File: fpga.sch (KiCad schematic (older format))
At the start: 8 parts, among them U601 XC7A35T-FGG484, U602 S25FL127S

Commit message: specify FPGA speed grade
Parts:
- U601: value XC7A35T-FGG484 -> XC7A35T-2FGG484
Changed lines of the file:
@@
 P 19500 4600
 F 0 "U601" H 19500 1626 50  0000 C CNN
-F 1 "XC7A35T-FGG484" H 19500 1535 50  0000 C CNN
+F 1 "XC7A35T-2FGG484" H 19500 1535 50  0000 C CNN
 F 2 "Package_BGA:BGA-484_23.0x23.0mm_Layout22x22_P1.0mm" H 19500 4600 50  0001 C CNN
 F 3 "" H 19500 4600 50  0000 C CNN
@@
 P 8400 11100
 F 0 "U601" H 8350 9850 50  0000 L CNN
-F 1 "XC7A35T-FGG484" H 8100 9750 50  0000 L CNN
+F 1 "XC7A35T-2FGG484" H 8100 9750 50  0000 L CNN
 F 2 "Package_BGA:BGA-484_23.0x23.0mm_Layout22x22_P1.0mm" H 8400 11100 50  0001 C CNN
 F 3 "" H 8400 11100 50  0000 C CNN
@@
 P 8400 14600
 F 0 "U601" H 8400 15267 50  0000 C CNN
-F 1 "XC7A35T-FGG484" H 8400 15176 50  0000 C CNN
+F 1 "XC7A35T-2FGG484" H 8400 15176 50  0000 C CNN
 F 2 "Package_BGA:BGA-484_23.0x23.0mm_Layout22x22_P1.0mm" H 8400 14600 50  0001 C CNN
 F 3 "" H 8400 14600 50  0000 C CNN
@@
 P 13800 13600
 F 0 "U601" H 13850 11950 50  0000 R CNN
-F 1 "XC7A35T-FGG484" H 14100 11850 50  0000 R CNN
+F 1 "XC7A35T-2FGG484" H 14100 11850 50  0000 R CNN
 F 2 "Package_BGA:BGA-484_23.0x23.0mm_Layout22x22_P1.0mm" H 13800 13600 50  0001 C CNN
 F 3 "" H 13800 13600 50  0000 C CNN
@@
 P 2600 12500
 F 0 "U601" H 2600 15667 50  0000 C CNN
-F 1 "XC7A35T-FGG484" H 2600 15576 50  0000 C CNN
+F 1 "XC7A35T-2FGG484" H 2600 15576 50  0000 C CNN
 F 2 "Package_BGA:BGA-484_23.0x23.0mm_Layout22x22_P1.0mm" H 2600 12500 50  0001 C CNN
 F 3 "" H 2600 12500 50  0000 C CNN
@@
 P 5500 4600
 F 0 "U601" H 5550 1650 50  0000 R CNN
-F 1 "XC7A35T-FGG484" H 5800 1550 50  0000 R CNN
+F 1 "XC7A35T-2FGG484" H 5800 1550 50  0000 R CNN
 F 2 "Package_BGA:BGA-484_23.0x23.0mm_Layout22x22_P1.0mm" H 5500 4600 50  0001 C CNN
 F 3 "" H 5500 4600 50  0000 C CNN
@@
 P 12800 4600
 F 0 "U601" H 12800 1626 50  0000 C CNN
-F 1 "XC7A35T-FGG484" H 12800 1535 50  0000 C CNN
+F 1 "XC7A35T-2FGG484" H 12800 1535 50  0000 C CNN
 F 2 "Package_BGA:BGA-484_23.0x23.0mm_Layout22x22_P1.0mm" H 12800 4600 50  0001 C CNN
 F 3 "" H 12800 4600 50  0000 C CNN

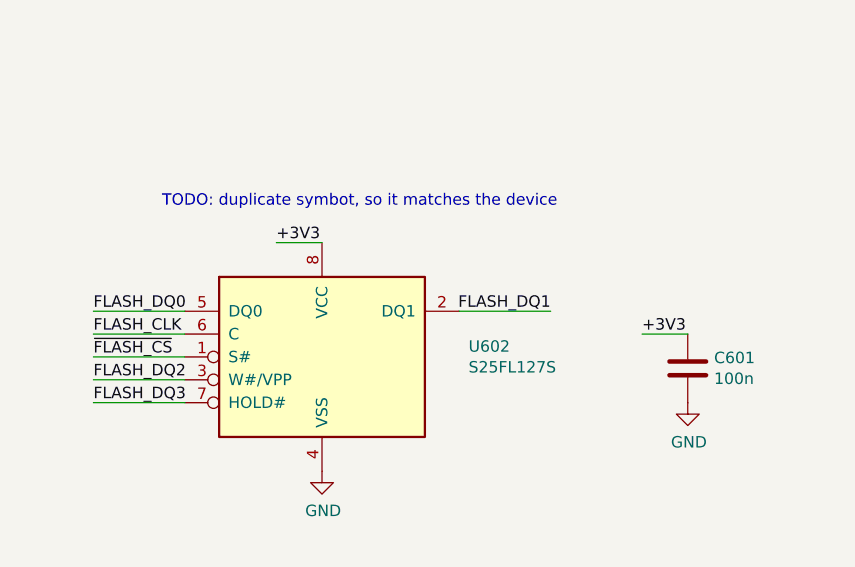
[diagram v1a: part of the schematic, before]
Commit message: specify exact part number of flash chip
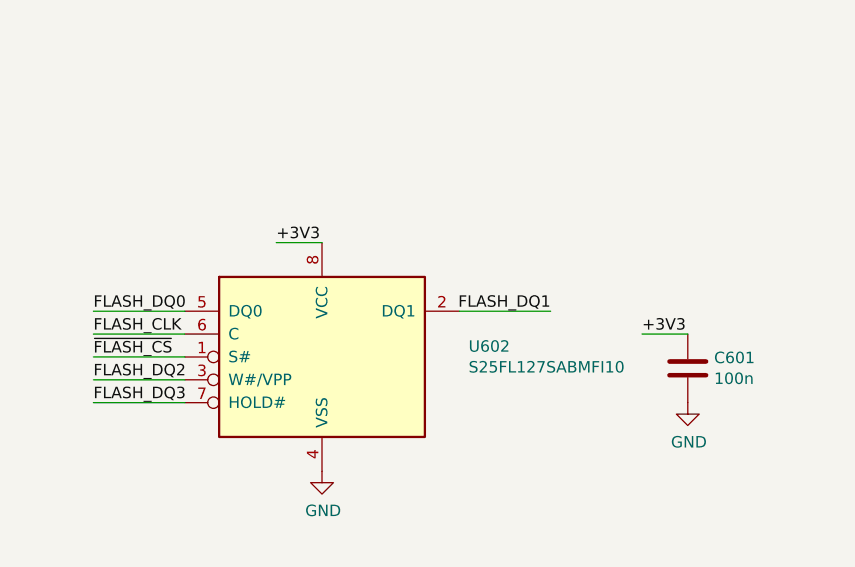
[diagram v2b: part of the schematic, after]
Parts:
- U602: value S25FL127S -> S25FL127SABMFI10
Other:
- note removed: "TODO: duplicate symbot, so it matches the device"
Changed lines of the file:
@@
 P 19500 12300
 F 0 "U602" H 20141 12346 50  0000 L CNN
-F 1 "S25FL127S" H 20141 12255 50  0000 L CNN
+F 1 "S25FL127SABMFI10" H 20141 12255 50  0000 L CNN
 F 2 "Package_SO:SOIJ-8_5.3x5.3mm_P1.27mm" H 20150 12350 50  0001 C CNN
-F 3 "https://www.micron.com/~/media/documents/products/data-sheet/nor-flash/serial-nor/m25px/m25px32.pdf" H 19650 12200 50  0001 C CNN
+F 3 "" H 19650 12200 50  0001 C CNN
 	1    19500 12300
 	1    0    0    -1
@@
 Wire Wire Line
 	21500 5200 21600 5200
-Text Notes 18800 11650 0    50   ~ 0
-TODO: duplicate symbot, so it matches the device
 NoConn ~ 21500 3300
 NoConn ~ 21500 3700

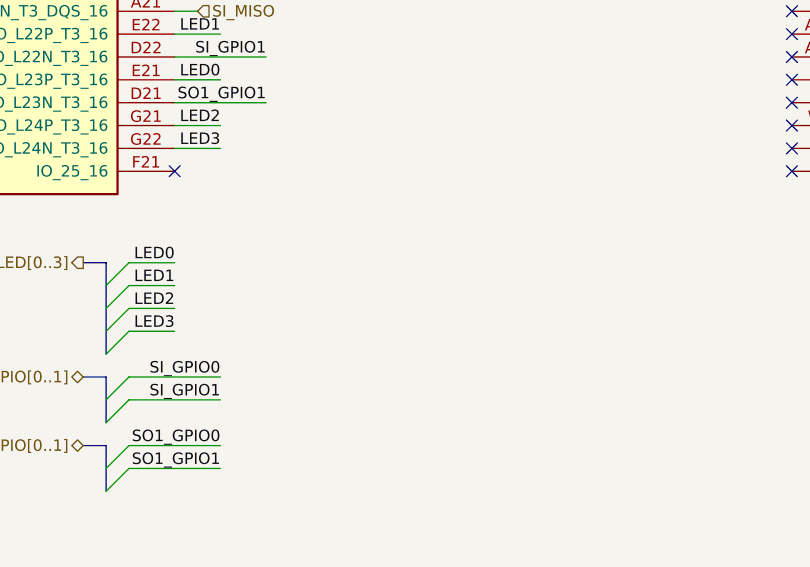
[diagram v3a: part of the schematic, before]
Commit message: connect leds to 3v3 power supply rail
the led is still connected to a 1v8 fpga io bank though
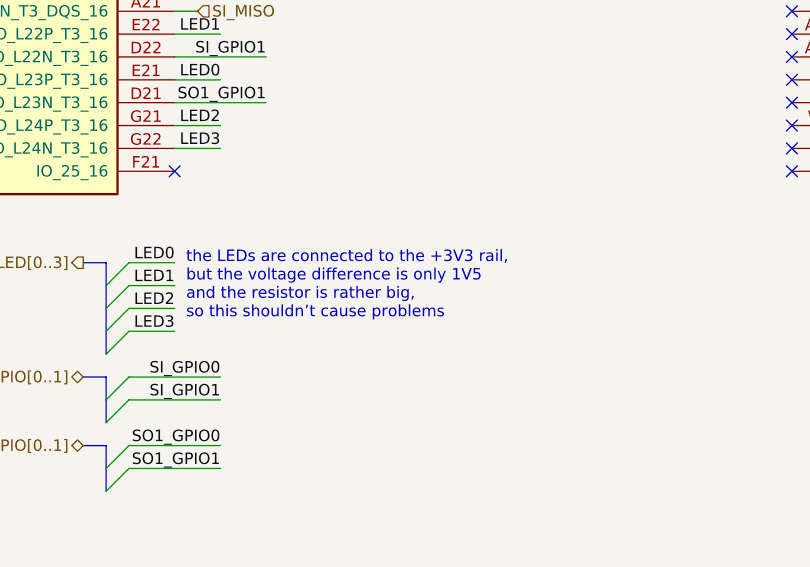
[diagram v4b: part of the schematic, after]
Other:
- note added: "the LEDs are connected to the +3V3 rail,\nbut the voltage difference is only 1V5\nand the resistor is rather big,\nso this shouldn’t cause problems"
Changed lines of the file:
@@
 Wire Bus Line
 	14500 7800 14500 8200
+Text Notes 14850 8050 0    50   ~ 0
+the LEDs are connected to the +3V3 rail,\nbut the voltage difference is only 1V5\nand the resistor is rather big,\nso this shouldn’t cause problems
 $EndSCHEMATC

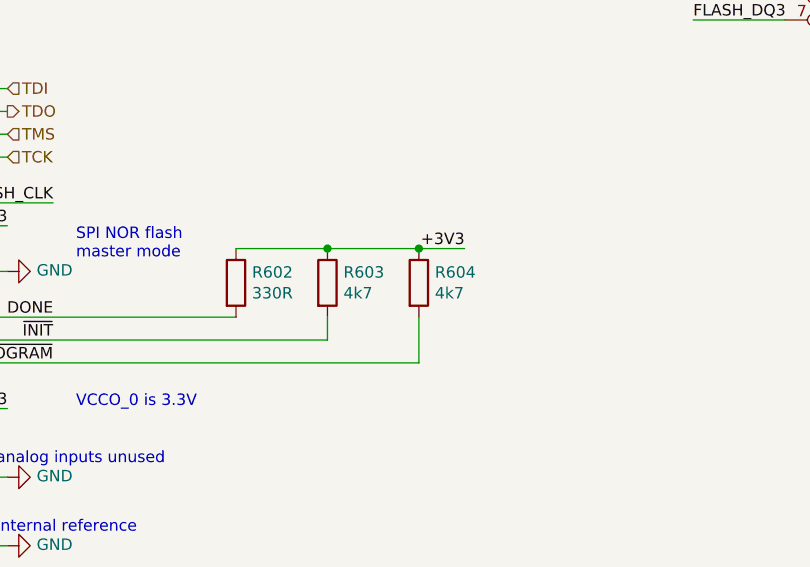
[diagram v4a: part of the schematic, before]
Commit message: fix moved plane bug, add init, done and power enable signals and optimize design
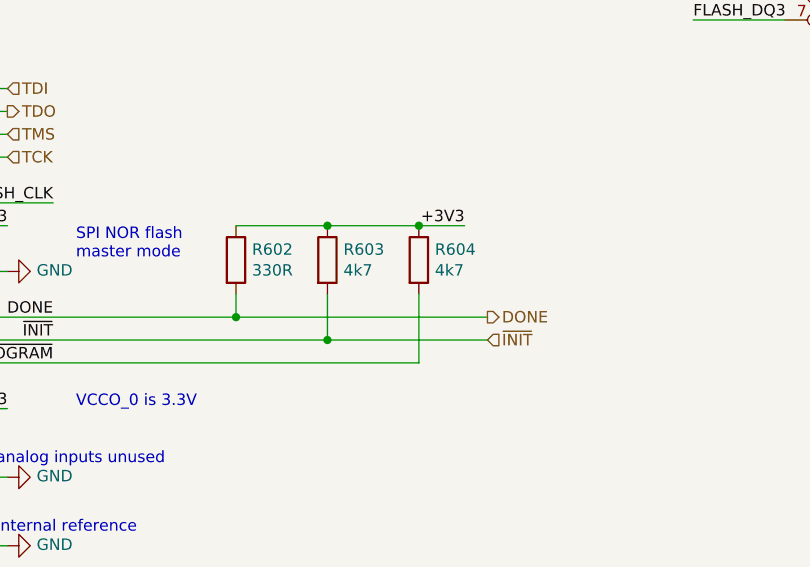
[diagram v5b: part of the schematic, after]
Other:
- moved on the sheet: R602, R603, R604
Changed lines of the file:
@@
 L Device:R R602
 U 1 1 5B3AC428
-P 16500 13650
-F 0 "R602" H 16570 13696 50  0000 L CNN
-F 1 "330R" H 16570 13605 50  0000 L CNN
-F 2 "Resistor_SMD:R_0402_1005Metric" V 16430 13650 50  0001 C CNN
-F 3 "~" H 16500 13650 50  0001 C CNN
-	1    16500 13650
+P 16500 13550
+F 0 "R602" H 16570 13596 50  0000 L CNN
+F 1 "330R" H 16570 13505 50  0000 L CNN
+F 2 "Resistor_SMD:R_0402_1005Metric" V 16430 13550 50  0001 C CNN
+F 3 "~" H 16500 13550 50  0001 C CNN
+	1    16500 13550
 	1    0    0    -1
 $EndComp
-Wire Wire Line
-	15300 13800 16500 13800
 $Comp
 L Device:R R603
 U 1 1 5B3F3344
-P 16900 13650
-F 0 "R603" H 16970 13696 50  0000 L CNN
-F 1 "4k7" H 16970 13605 50  0000 L CNN
-F 2 "Resistor_SMD:R_0402_1005Metric" V 16830 13650 50  0001 C CNN
-F 3 "~" H 16900 13650 50  0001 C CNN
-	1    16900 13650
+P 16900 13550
+F 0 "R603" H 16970 13596 50  0000 L CNN
+F 1 "4k7" H 16970 13505 50  0000 L CNN
+F 2 "Resistor_SMD:R_0402_1005Metric" V 16830 13550 50  0001 C CNN
+F 3 "~" H 16900 13550 50  0001 C CNN
+	1    16900 13550
 	1    0    0    -1
 $EndComp
@@
 L Device:R R604
 U 1 1 5B416F10
-P 17300 13650
-F 0 "R604" H 17370 13696 50  0000 L CNN
-F 1 "4k7" H 17370 13605 50  0000 L CNN
-F 2 "Resistor_SMD:R_0402_1005Metric" V 17230 13650 50  0001 C CNN
-F 3 "~" H 17300 13650 50  0001 C CNN
-	1    17300 13650
+P 17300 13550
+F 0 "R604" H 17370 13596 50  0000 L CNN
+F 1 "4k7" H 17370 13505 50  0000 L CNN
+F 2 "Resistor_SMD:R_0402_1005Metric" V 17230 13550 50  0001 C CNN
+F 3 "~" H 17300 13550 50  0001 C CNN
+	1    17300 13550
 	1    0    0    -1
 $EndComp
@@
 +1V0
 Wire Wire Line
-	16500 13500 16900 13500
-Wire Wire Line
-	16900 13500 17300 13500
-Connection ~ 16900 13500
-Wire Wire Line
-	17300 13500 17500 13500
-Connection ~ 17300 13500
-Text Label 17500 13500 2    50   ~ 0
-+3V3
-Wire Wire Line
-	16900 13900 16900 13800
-Wire Wire Line
-	17300 14000 17300 13800
+	16500 13400 16900 13400
+Wire Wire Line
+	16900 13400 17300 13400
+Connection ~ 16900 13400
+Wire Wire Line
+	17300 13400 17500 13400
+Connection ~ 17300 13400
+Text Label 17500 13400 2    50   ~ 0
++3V3
+Wire Wire Line
+	16900 13900 16900 13700
+Wire Wire Line
+	17300 14000 17300 13700
 Text Label 14600 11900 0    50   ~ 0
 +3V3
@@
 Wire Wire Line
 	21500 6700 21600 6700
-Wire Bus Line
-	14500 8600 14500 8800
-Wire Bus Line
-	21000 7800 21000 8000
-Wire Bus Line
-	14500 8300 14500 8500
-Wire Bus Line
-	14500 7800 14500 8200
 Text Notes 14850 8050 0    50   ~ 0
 the LEDs are connected to the +3V3 rail,\nbut the voltage difference is only 1V5\nand the resistor is rather big,\nso this shouldn’t cause problems
+Text HLabel 17600 13900 2    50   Input ~ 0
+~INIT
+Wire Wire Line
+	16900 13900 17600 13900
+Connection ~ 16900 13900
+Text HLabel 17600 13800 2    50   Output ~ 0
+DONE
+Wire Wire Line
+	15300 13800 16500 13800
+Wire Wire Line
+	16500 13700 16500 13800
+Connection ~ 16500 13800
+Wire Wire Line
+	16500 13800 17600 13800
+Wire Bus Line
+	14500 8600 14500 8800
+Wire Bus Line
+	21000 7800 21000 8000
+Wire Bus Line
+	14500 8300 14500 8500
+Wire Bus Line
+	14500 7800 14500 8200
 $EndSCHEMATC

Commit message: add 3 resistor footprints to configure a board ID to be able to detect revision and features present
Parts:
- added R602, R603, R604: 100R, Resistor_SMD:R_0402_1005Metric, symbol Device:R
- renumbered R602 to R605, R603 to R606, R604 to R607, R605 to R608
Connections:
- net GND: now also R602.1, R603.1, R604.1
- net BOARD_ID_2: now reaches U601.V18 (IO_L14P_T2_SRCC_14)
- net BOARD_ID_2: now also R604.2
- net BOARD_ID_1: now reaches U601.Y18 (IO_L13P_T2_MRCC_14)
- net BOARD_ID_1: now also R602.2
- net BOARD_ID_0: now reaches U601.Y19 (IO_L13N_T2_MRCC_14)
- net BOARD_ID_0: now also R603.2
- no-connect marks 190 -> 187
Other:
- note added: "populate these depending on the board ID"
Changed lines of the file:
@@
 $EndComp
 $Comp
-L power:GND #PWR0613
+L power:GND #PWR0616
 U 1 1 5AEC478C
 P 1500 15500
-F 0 "#PWR0613" H 1500 15250 50  0001 C CNN
+F 0 "#PWR0616" H 1500 15250 50  0001 C CNN
 F 1 "GND" H 1505 15327 50  0000 C CNN
 F 2 "" H 1500 15500 50  0001 C CNN
@@
 	1500 15400 1500 15500
 $Comp
-L power:GND #PWR0614
+L power:GND #PWR0617
 U 1 1 5AED823A
 P 3700 15500
-F 0 "#PWR0614" H 3700 15250 50  0001 C CNN
+F 0 "#PWR0617" H 3700 15250 50  0001 C CNN
 F 1 "GND" H 3705 15327 50  0000 C CNN
 F 2 "" H 3700 15500 50  0001 C CNN
@@
 	3700 15400 3700 15500
 $Comp
-L Device:R R605
+L Device:R R608
 U 1 1 5AF685FD
 P 10650 14900
-F 0 "R605" V 10443 14900 50  0000 C CNN
+F 0 "R608" V 10443 14900 50  0000 C CNN
 F 1 "100R" V 10534 14900 50  0000 C CNN
 F 2 "Resistor_SMD:R_0201_0603Metric" V 10580 14900 50  0001 C CNN
@@
 	15300 13400 15500 13400
 $Comp
-L power:GND #PWR0610
+L power:GND #PWR0613
 U 1 1 5B037925
 P 15500 13600
-F 0 "#PWR0610" H 15500 13350 50  0001 C CNN
+F 0 "#PWR0613" H 15500 13350 50  0001 C CNN
 F 1 "GND" V 15505 13472 50  0000 R CNN
 F 2 "" H 15500 13600 50  0001 C CNN
@@
 NoConn ~ 14800 3300
 $Comp
-L power:GND #PWR0606
+L power:GND #PWR0609
 U 1 1 5B5B64DE
 P 6800 11500
-F 0 "#PWR0606" H 6800 11250 50  0001 C CNN
+F 0 "#PWR0609" H 6800 11250 50  0001 C CNN
 F 1 "GND" V 6805 11372 50  0000 R CNN
 F 2 "" H 6800 11500 50  0001 C CNN
@@
 $EndComp
 $Comp
-L power:GND #PWR0607
+L power:GND #PWR0610
 U 1 1 5B5B6565
 P 6800 11600
-F 0 "#PWR0607" H 6800 11350 50  0001 C CNN
+F 0 "#PWR0610" H 6800 11350 50  0001 C CNN
 F 1 "GND" V 6805 11472 50  0000 R CNN
 F 2 "" H 6800 11600 50  0001 C CNN
@@
 $EndComp
 $Comp
-L power:GND #PWR0604
+L power:GND #PWR0607
 U 1 1 5B5B6582
 P 6800 11100
-F 0 "#PWR0604" H 6800 10850 50  0001 C CNN
+F 0 "#PWR0607" H 6800 10850 50  0001 C CNN
 F 1 "GND" V 6805 10972 50  0000 R CNN
 F 2 "" H 6800 11100 50  0001 C CNN
@@
 $EndComp
 $Comp
-L power:GND #PWR0605
+L power:GND #PWR0608
 U 1 1 5B5B659F
 P 6800 11200
-F 0 "#PWR0605" H 6800 10950 50  0001 C CNN
+F 0 "#PWR0608" H 6800 10950 50  0001 C CNN
 F 1 "GND" V 6805 11072 50  0000 R CNN
 F 2 "" H 6800 11200 50  0001 C CNN
@@
 $EndComp
 $Comp
-L power:GND #PWR0609
+L power:GND #PWR0612
 U 1 1 5AFE504F
 P 19500 12800
-F 0 "#PWR0609" H 19500 12550 50  0001 C CNN
+F 0 "#PWR0612" H 19500 12550 50  0001 C CNN
 F 1 "GND" H 19505 12627 50  0000 C CNN
 F 2 "" H 19500 12800 50  0001 C CNN
@@
 $EndComp
 $Comp
-L power:GND #PWR0608
+L power:GND #PWR0611
 U 1 1 5AFE56CA
 P 21100 12500
-F 0 "#PWR0608" H 21100 12250 50  0001 C CNN
+F 0 "#PWR0611" H 21100 12250 50  0001 C CNN
 F 1 "GND" H 21105 12327 50  0000 C CNN
 F 2 "" H 21100 12500 50  0001 C CNN
@@
 ~FLASH_CS
 $Comp
-L power:GND #PWR0612
+L power:GND #PWR0615
 U 1 1 5B0155B6
 P 15500 14800
-F 0 "#PWR0612" H 15500 14550 50  0001 C CNN
+F 0 "#PWR0615" H 15500 14550 50  0001 C CNN
 F 1 "GND" V 15505 14672 50  0000 R CNN
 F 2 "" H 15500 14800 50  0001 C CNN
@@
 internal reference
 $Comp
-L power:GND #PWR0602
+L power:GND #PWR0605
 U 1 1 5B074A2B
 P 1400 10200
-F 0 "#PWR0602" H 1400 9950 50  0001 C CNN
+F 0 "#PWR0605" H 1400 9950 50  0001 C CNN
 F 1 "GND" V 1405 10072 50  0000 R CNN
 F 2 "" H 1400 10200 50  0001 C CNN
@@
 	1600 10200 1400 10200
 $Comp
-L power:GND #PWR0611
+L power:GND #PWR0614
 U 1 1 5B0BD6A0
 P 15500 14500
-F 0 "#PWR0611" H 15500 14250 50  0001 C CNN
+F 0 "#PWR0614" H 15500 14250 50  0001 C CNN
 F 1 "GND" V 15505 14372 50  0000 R CNN
 F 2 "" H 15500 14500 50  0001 C CNN
@@
 NoConn ~ 7500 5700
 $Comp
-L power:GND #PWR0603
+L power:GND #PWR0606
 U 1 1 5B267380
 P 1400 10400
-F 0 "#PWR0603" H 1400 10150 50  0001 C CNN
+F 0 "#PWR0606" H 1400 10150 50  0001 C CNN
 F 1 "GND" V 1405 10272 50  0000 R CNN
 F 2 "" H 1400 10400 50  0001 C CNN
@@
 ~PROGRAM
 $Comp
-L Device:R R602
+L Device:R R605
 U 1 1 5B3AC428
 P 16500 13550
-F 0 "R602" H 16570 13596 50  0000 L CNN
+F 0 "R605" H 16570 13596 50  0000 L CNN
 F 1 "330R" H 16570 13505 50  0000 L CNN
 F 2 "Resistor_SMD:R_0402_1005Metric" V 16430 13550 50  0001 C CNN
@@
 $EndComp
 $Comp
-L Device:R R603
+L Device:R R606
 U 1 1 5B3F3344
 P 16900 13550
-F 0 "R603" H 16970 13596 50  0000 L CNN
+F 0 "R606" H 16970 13596 50  0000 L CNN
 F 1 "4k7" H 16970 13505 50  0000 L CNN
 F 2 "Resistor_SMD:R_0402_1005Metric" V 16830 13550 50  0001 C CNN
@@
 	15300 13900 16900 13900
 $Comp
-L Device:R R604
+L Device:R R607
 U 1 1 5B416F10
 P 17300 13550
-F 0 "R604" H 17370 13596 50  0000 L CNN
+F 0 "R607" H 17370 13596 50  0000 L CNN
 F 1 "4k7" H 17370 13505 50  0000 L CNN
 F 2 "Resistor_SMD:R_0402_1005Metric" V 17230 13550 50  0001 C CNN
@@
 Text HLabel 21600 6500 2    50   Output ~ 0
 REFCLK_N
-$Comp
-L FPGA_Xilinx_Artix7:XC7A35T-FGG484 U601
-U 1 1 5AEC3F9D
-P 5500 4600
-F 0 "U601" H 5550 1650 50  0000 R CNN
-F 1 "XC7A35T-2FGG484" H 5800 1550 50  0000 R CNN
-F 2 "Package_BGA:BGA-484_23.0x23.0mm_Layout22x22_P1.0mm" H 5500 4600 50  0001 C CNN
-F 3 "" H 5500 4600 50  0000 C CNN
-	1    5500 4600
-	1    0    0    -1
-$EndComp
 Wire Wire Line
 	17400 2600 17500 2600
@@
 NoConn ~ 7500 4800
 NoConn ~ 7500 4900
-NoConn ~ 7500 5000
-NoConn ~ 7500 5100
-NoConn ~ 7500 5200
 NoConn ~ 7500 5300
 Wire Wire Line
@@
 Wire Wire Line
 	16500 13800 17600 13800
+$Comp
+L Device:R R603
+U 1 1 5C466907
+P 8150 5100
+F 0 "R603" V 7943 5100 50  0000 C CNN
+F 1 "100R" V 8034 5100 50  0000 C CNN
+F 2 "Resistor_SMD:R_0402_1005Metric" V 8080 5100 50  0001 C CNN
+F 3 "~" H 8150 5100 50  0001 C CNN
+	1    8150 5100
+	0    1    -1   0
+$EndComp
+$Comp
+L Device:R R602
+U 1 1 5C468A3D
+P 8150 4800
+F 0 "R602" V 7943 4800 50  0000 C CNN
+F 1 "100R" V 8034 4800 50  0000 C CNN
+F 2 "Resistor_SMD:R_0402_1005Metric" V 8080 4800 50  0001 C CNN
+F 3 "~" H 8150 4800 50  0001 C CNN
+	1    8150 4800
+	0    1    -1   0
+$EndComp
+$Comp
+L Device:R R604
+U 1 1 5C468BD2
+P 8150 5400
+F 0 "R604" V 7943 5400 50  0000 C CNN
+F 1 "100R" V 8034 5400 50  0000 C CNN
+F 2 "Resistor_SMD:R_0402_1005Metric" V 8080 5400 50  0001 C CNN
+F 3 "~" H 8150 5400 50  0001 C CNN
+	1    8150 5400
+	0    1    -1   0
+$EndComp
+$Comp
+L power:GND #PWR0603
+U 1 1 5C46929C
+P 8300 5100
+F 0 "#PWR0603" H 8300 4850 50  0001 C CNN
+F 1 "GND" V 8305 4972 50  0000 R CNN
+F 2 "" H 8300 5100 50  0001 C CNN
+F 3 "" H 8300 5100 50  0001 C CNN
+	1    8300 5100
+	0    -1   -1   0
+$EndComp
+$Comp
+L power:GND #PWR0602
+U 1 1 5C4694BD
+P 8300 4800
+F 0 "#PWR0602" H 8300 4550 50  0001 C CNN
+F 1 "GND" V 8305 4672 50  0000 R CNN
+F 2 "" H 8300 4800 50  0001 C CNN
+F 3 "" H 8300 4800 50  0001 C CNN
+	1    8300 4800
+	0    -1   -1   0
+$EndComp
+$Comp
+L power:GND #PWR0604
+U 1 1 5C46969A
+P 8300 5400
+F 0 "#PWR0604" H 8300 5150 50  0001 C CNN
+F 1 "GND" V 8305 5272 50  0000 R CNN
+F 2 "" H 8300 5400 50  0001 C CNN
+F 3 "" H 8300 5400 50  0001 C CNN
+	1    8300 5400
+	0    -1   -1   0
+$EndComp
+$Comp
+L FPGA_Xilinx_Artix7:XC7A35T-FGG484 U601
+U 1 1 5AEC3F9D
+P 5500 4600
+F 0 "U601" H 5550 1650 50  0000 R CNN
+F 1 "XC7A35T-2FGG484" H 5800 1550 50  0000 R CNN
+F 2 "Package_BGA:BGA-484_23.0x23.0mm_Layout22x22_P1.0mm" H 5500 4600 50  0001 C CNN
+F 3 "" H 5500 4600 50  0000 C CNN
+	1    5500 4600
+	1    0    0    -1
+$EndComp
+Wire Wire Line
+	7500 5000 8000 5000
+Wire Wire Line
+	7500 5100 8000 5100
+Wire Wire Line
+	7500 5200 8000 5200
+Text Label 7500 5100 0    50   ~ 0
+BOARD_ID_0
+Wire Wire Line
+	8000 5000 8000 4800
+Text Label 7500 5000 0    50   ~ 0
+BOARD_ID_1
+Wire Wire Line
+	8000 5200 8000 5400
+Text Label 7500 5200 0    50   ~ 0
+BOARD_ID_2
+Wire Notes Line
+	7950 5650 8300 5650
+Wire Notes Line
+	8300 5650 8300 4700
+Wire Notes Line
+	8300 4700 7950 4700
+Wire Notes Line
+	7950 4700 7950 5650
 Wire Bus Line
 	14500 8600 14500 8800
@@
 Wire Bus Line
 	14500 7800 14500 8200
+Text Notes 7700 4650 0    50   ~ 0
+populate these depending on the board ID
 $EndSCHEMATC
